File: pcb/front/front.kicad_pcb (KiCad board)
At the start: 4 copper layers, 26.5 x 26.5 mm, 187 parts

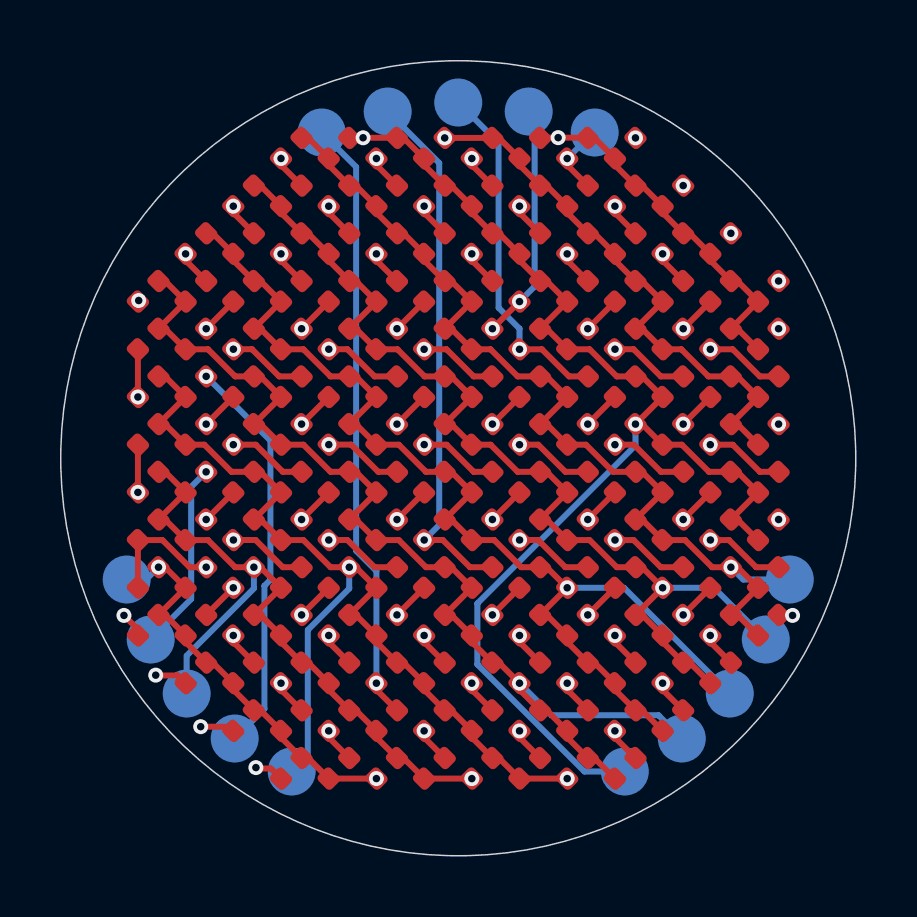
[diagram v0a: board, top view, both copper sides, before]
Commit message: Add tooling holes
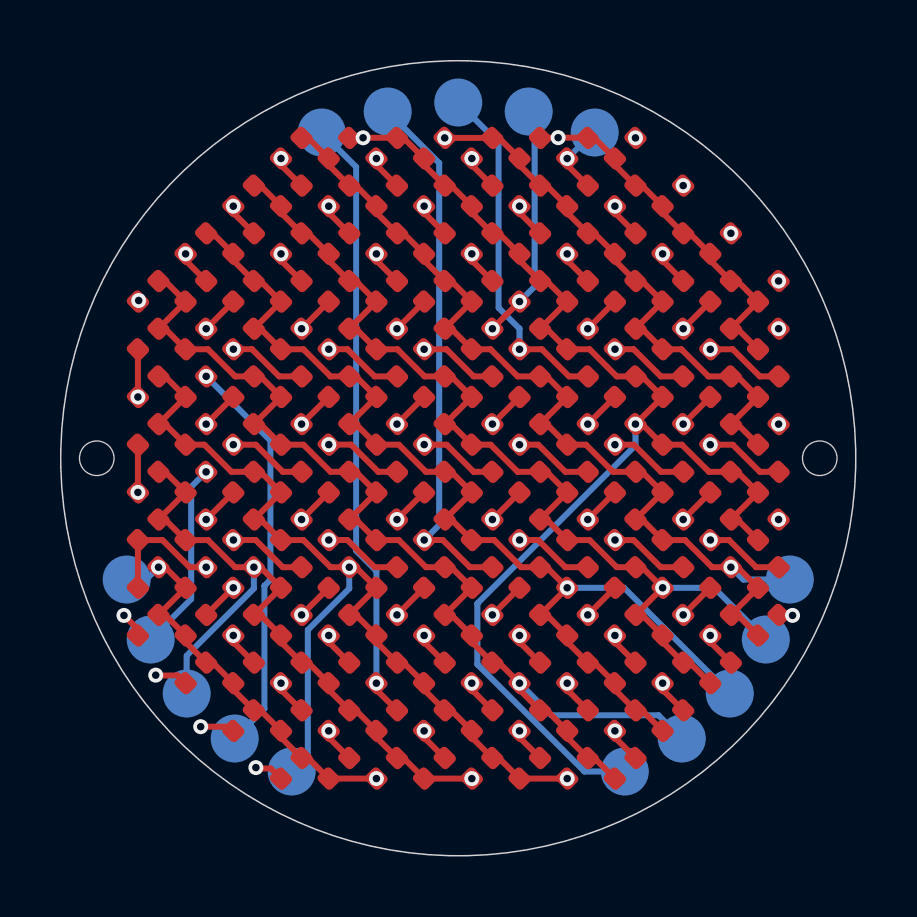
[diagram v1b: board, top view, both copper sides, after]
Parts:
- added REF**: ToolingHole_1.152mm, MountingHole:ToolingHole_1.152mm, F.Cu at (160.0, 89.5)
- added REF**: ToolingHole_1.152mm, MountingHole:ToolingHole_1.152mm, F.Cu at (135.9, 89.5)
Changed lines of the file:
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@@
 		)
 	)
+	(footprint "MountingHole:ToolingHole_1.152mm"
+		(layer "F.Cu")
+		(at 159.985 89.525)
+		(descr "Tooling Hole 1.152mm, 1.3mm solder mask, JLCPCB specification, https://jlcpcb.com/help/article/How-to-add-tooling-holes-for-PCB-assembly-order")
+		(tags "mounting")
+		(property "Reference" "REF**"
+			(at 0 -1.5 0)
+			(layer "F.SilkS")
+			(hide yes)
+			(effects
+				(font
+					(size 1 1)
+					(thickness 0.15)
+				)
+			)
+		)
+		(property "Value" "ToolingHole_1.152mm"
+			(at 0 1.6 0)
+			(layer "F.Fab")
+			(effects
+				(font
+					(size 1 1)
+					(thickness 0.15)
+				)
+			)
+		)
+		(property "Datasheet" ""
+			(at 0 0 0)
+			(unlocked yes)
+			(layer "F.Fab")
+			(hide yes)
+			(effects
+				(font
+					(size 1.27 1.27)
+					(thickness 0.15)
+				)
+			)
+		)
+		(property "Description" ""
+			(at 0 0 0)
+			(unlocked yes)
+			(layer "F.Fab")
+			(hide yes)
+			(effects
+				(font
+					(size 1.27 1.27)
+					(thickness 0.15)
+				)
+			)
+		)
+		(attr exclude_from_pos_files exclude_from_bom)
+		(duplicate_pad_numbers_are_jumpers no)
+		(fp_circle
+			(center 0 0)
+			(end 0.7 0)
+			(stroke
+				(width 0.05)
+				(type solid)
+			)
+			(fill no)
+			(layer "F.CrtYd")
+		)
+		(fp_text user "${REFERENCE}"
+			(at 0 0 0)
+			(layer "F.Fab")
+			(effects
+				(font
+					(size 1 1)
+					(thickness 0.15)
+				)
+			)
+		)
+		(pad "" np_thru_hole circle
+			(at 0 0)
+			(size 1.152 1.152)
+			(drill 1.152)
+			(layers "*.Cu" "*.Mask")
+			(solder_mask_margin 0.074)
+		)
+		(zone
+			(layers "F.Cu" "B.Cu" "In1.Cu" "In2.Cu")
+			(hatch edge 0.5)
+			(connect_pads
+				(clearance 0)
+			)
+			(min_thickness 0.25)
+			(keepout
+				(tracks not_allowed)
+				(vias allowed)
+				(pads allowed)
+				(copperpour not_allowed)
+				(footprints not_allowed)
+			)
+			(placement
+				(enabled no)
+				(sheetname "")
+			)
+			(fill
+				(thermal_gap 0.5)
+				(thermal_bridge_width 0.5)
+				(island_removal_mode 0)
+			)
+			(polygon
+				(pts
+					(xy 160.685 89.525) (xy 160.664659 89.357479) (xy 160.604819 89.199694) (xy 160.508958 89.060814)
+					(xy 160.382645 88.948911) (xy 160.233223 88.870489) (xy 160.069376 88.830104) (xy 159.900624 88.830104)
+					(xy 159.736777 88.870489) (xy 159.587355 88.948911) (xy 159.461042 89.060814) (xy 159.365181 89.199694)
+					(xy 159.305341 89.357479) (xy 159.285 89.525) (xy 159.305341 89.692521) (xy 159.365181 89.850306)
+					(xy 159.461042 89.989186) (xy 159.587355 90.101089) (xy 159.736777 90.179511) (xy 159.900624 90.219896)
+					(xy 160.069376 90.219896) (xy 160.233223 90.179511) (xy 160.382645 90.101089) (xy 160.508958 89.989186)
+					(xy 160.604819 89.850306) (xy 160.664659 89.692521)
+				)
+			)
+		)
+		(embedded_fonts no)
+	)
 	(footprint "Project:LED_0402_1005Metric"
 		(layer "F.Cu")
@@
 		)
 	)
+	(footprint "MountingHole:ToolingHole_1.152mm"
+		(layer "F.Cu")
+		(at 135.885 89.525)
+		(descr "Tooling Hole 1.152mm, 1.3mm solder mask, JLCPCB specification, https://jlcpcb.com/help/article/How-to-add-tooling-holes-for-PCB-assembly-order")
+		(tags "mounting")
+		(property "Reference" "REF**"
+			(at 0 -1.5 0)
+			(layer "F.SilkS")
+			(hide yes)
+			(effects
+				(font
+					(size 1 1)
+					(thickness 0.15)
+				)
+			)
+		)
+		(property "Value" "ToolingHole_1.152mm"
+			(at 0 1.6 0)
+			(layer "F.Fab")
+			(effects
+				(font
+					(size 1 1)
+					(thickness 0.15)
+				)
+			)
+		)
+		(property "Datasheet" ""
+			(at 0 0 0)
+			(unlocked yes)
+			(layer "F.Fab")
+			(hide yes)
+			(effects
+				(font
+					(size 1.27 1.27)
+					(thickness 0.15)
+				)
+			)
+		)
+		(property "Description" ""
+			(at 0 0 0)
+			(unlocked yes)
+			(layer "F.Fab")
+			(hide yes)
+			(effects
+				(font
+					(size 1.27 1.27)
+					(thickness 0.15)
+				)
+			)
+		)
+		(attr exclude_from_pos_files exclude_from_bom)
+		(duplicate_pad_numbers_are_jumpers no)
+		(fp_circle
+			(center 0 0)
+			(end 0.7 0)
+			(stroke
+				(width 0.05)
+				(type solid)
+			)
+			(fill no)
+			(layer "F.CrtYd")
+		)
+		(fp_text user "${REFERENCE}"
+			(at 0 0 0)
+			(layer "F.Fab")
+			(effects
+				(font
+					(size 1 1)
+					(thickness 0.15)
+				)
+			)
+		)
+		(pad "" np_thru_hole circle
+			(at 0 0)
+			(size 1.152 1.152)
+			(drill 1.152)
+			(layers "*.Cu" "*.Mask")
+			(solder_mask_margin 0.074)
+		)
+		(zone
+			(layers "F.Cu" "B.Cu" "In1.Cu" "In2.Cu")
+			(hatch edge 0.5)
+			(connect_pads
+				(clearance 0)
+			)
+			(min_thickness 0.25)
+			(keepout
+				(tracks not_allowed)
+				(vias allowed)
+				(pads allowed)
+				(copperpour not_allowed)
+				(footprints not_allowed)
+			)
+			(placement
+				(enabled no)
+				(sheetname "")
+			)
+			(fill
+				(thermal_gap 0.5)
+				(thermal_bridge_width 0.5)
+				(island_removal_mode 0)
+			)
+			(polygon
+				(pts
+					(xy 136.585 89.525) (xy 136.564659 89.357479) (xy 136.504819 89.199694) (xy 136.408958 89.060814)
+					(xy 136.282645 88.948911) (xy 136.133223 88.870489) (xy 135.969376 88.830104) (xy 135.800624 88.830104)
+					(xy 135.636777 88.870489) (xy 135.487355 88.948911) (xy 135.361042 89.060814) (xy 135.265181 89.199694)
+					(xy 135.205341 89.357479) (xy 135.185 89.525) (xy 135.205341 89.692521) (xy 135.265181 89.850306)
+					(xy 135.361042 89.989186) (xy 135.487355 90.101089) (xy 135.636777 90.179511) (xy 135.800624 90.219896)
+					(xy 135.969376 90.219896) (xy 136.133223 90.179511) (xy 136.282645 90.101089) (xy 136.408958 89.989186)
+					(xy 136.504819 89.850306) (xy 136.564659 89.692521)
+				)
+			)
+		)
+		(embedded_fonts no)
+	)
 	(footprint "Project:LED_0402_1005Metric"
